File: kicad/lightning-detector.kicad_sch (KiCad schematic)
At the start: 26 parts, among them J1 PWR, J2 Conn_Coaxial, J3 PWR, J4 PWR, J5 RF Detect, U1 NUCLEO-L432KC, U2 AZ1117H-ADJ, U3 TPS61023DRLR

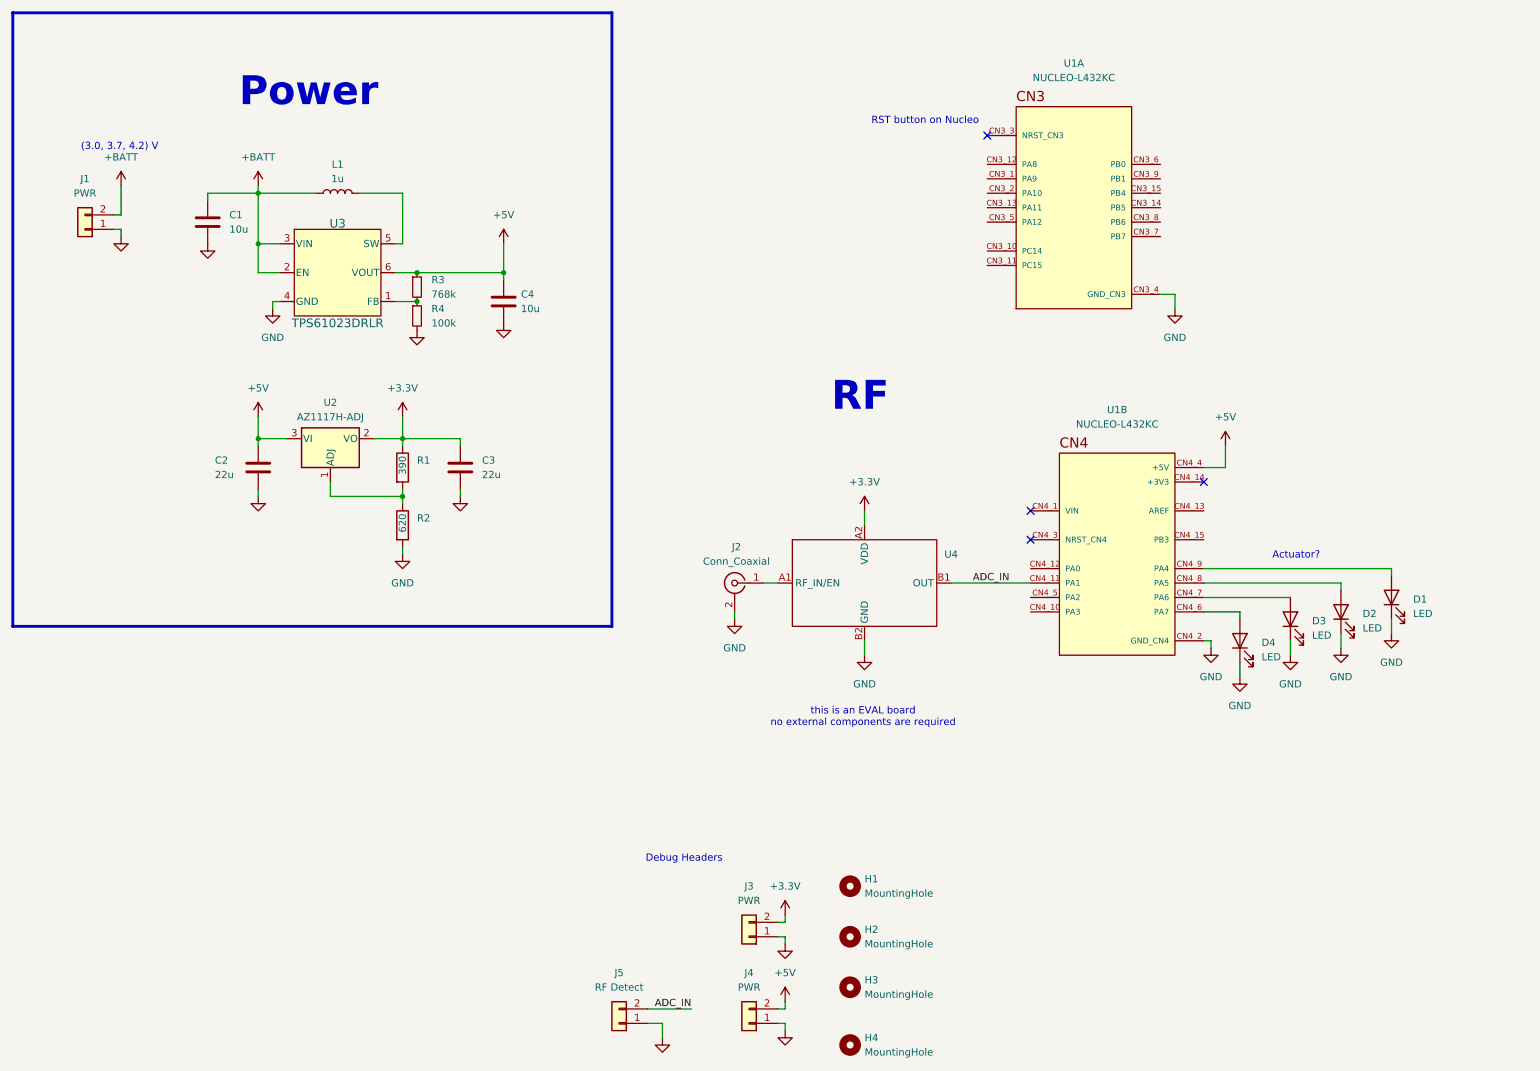
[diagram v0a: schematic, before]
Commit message: Updated schematic and created preliminary PCB.
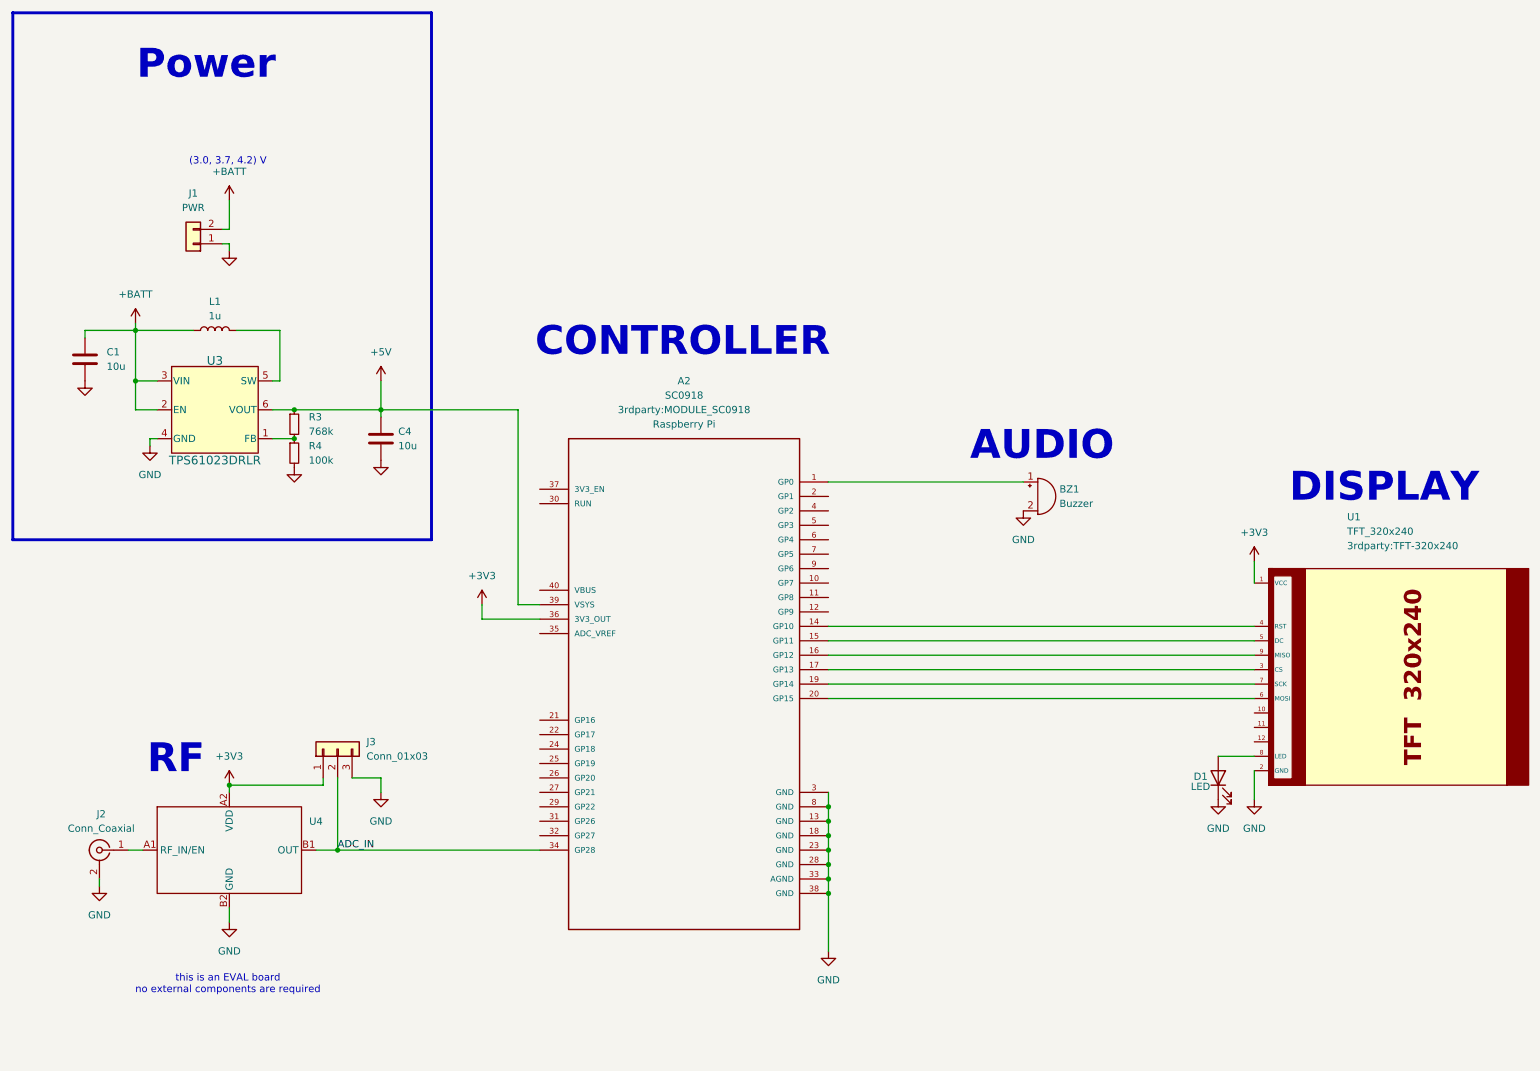
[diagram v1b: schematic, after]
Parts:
- removed C2, C3: 22u, Capacitor_SMD:C_0603_1608Metric, symbol Device:C
- removed D2, D3, D4: LED, symbol Device:LED
- removed H1, H2, H3, H4: MountingHole, MountingHole:MountingHole_4.3mm_M4, symbol Mechanical:MountingHole
- removed J3, J4: PWR, Connector_PinHeader_2.54mm:PinHeader_1x02_P2.54mm_Vertical, symbol Connector_Generic:Conn_01x02
- removed J5: RF Detect, Connector_PinHeader_2.54mm:PinHeader_1x02_P2.54mm_Vertical, symbol Connector_Generic:Conn_01x02
- removed R1: 390, Resistor_SMD:R_0603_1608Metric, symbol Device:R
- removed R2: 620, Resistor_SMD:R_0603_1608Metric, symbol Device:R
- removed U1: NUCLEO-L432KC, NUCLEO-L432KC:MODULE_NUCLEO-L432KC, symbol NUCLEO-L432KC:NUCLEO-L432KC
- removed U2: AZ1117H-ADJ, Package_TO_SOT_SMD:SOT-223-3_TabPin2, symbol Regulator_Linear:AZ1117H-ADJ
- added A2: SC0918, 3rdparty:MODULE_SC0918, symbol Raspberry_Pi_Pico_W_SC0918:SC0918
- added BZ1: Buzzer, Buzzer_Beeper:Buzzer_12x9.5RM7.6, symbol Device:Buzzer
- added J3: Conn_01x03, Connector_PinHeader_2.54mm:PinHeader_1x03_P2.54mm_Vertical, symbol Connector_Generic:Conn_01x03
- added U1: TFT_320x240, 3rdparty:TFT-320x240, symbol tft_320x240:TFT_320x240
- D1: footprint (none) -> LED_THT:LED_D3.0mm
- U3: footprint DRL0006A -> 3rdparty:SOT563-ORI
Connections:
- net +5V: now also A2.39 (VSYS)
- net ADC_IN: now also A2.34 (GP28), J3.2 (Pin_2)
- net GND: now also A2.13 (GND), A2.18 (GND), A2.23 (GND), A2.28 (GND), A2.3 (GND), A2.33 (AGND), A2.38 (GND), A2.8 (GND), BZ1.2 (-), J3.3 (Pin_3), U1.2 (GND)
- net at D1.2 (A): now also U1.8 (LED)
- net +3.3V renamed +3V3
- net +3V3: now also A2.36 (3V3_OUT), J3.1 (Pin_1), U1.1 (VCC)
- new net: A2.1 (GP0), BZ1.1 (+)
- new net: A2.14 (GP10), U1.4 (RST)
- new net: A2.15 (GP11), U1.5 (DC)
- new net: A2.16 (GP12), U1.9 (MISO)
- new net: A2.17 (GP13), U1.3 (CS)
- new net: A2.19 (GP14), U1.7 (SCK)
- new net: A2.20 (GP15), U1.6 (MOSI)
- no-connect marks 4 -> 0
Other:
- note added: "AUDIO"
- note added: "CONTROLLER"
- note added: "DISPLAY"
- note removed: "Actuator?"
- note removed: "Debug Headers"
- note removed: "RST button on Nucleo"
- moved on the sheet: C1, C4, J1, J2, L1, R3, R4, U3, U4

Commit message: wk07 items
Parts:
- removed D1: LED, LED_THT:LED_D3.0mm, symbol Device:LED
- removed U1: TFT_320x240, 3rdparty:TFT-320x240, symbol tft_320x240:TFT_320x240
- added J4: ADF7020 Breakout, Connector_IDC:IDC-Header_2x07_P2.54mm_Vertical, symbol Connector_Generic:Conn_02x07_Top_Bottom
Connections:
- net +3V3: now also J4.3 (Pin_3)
- net GND: now also J4.2 (Pin_2)
- net CLKOUT: now reaches A2.14 (GP10)
- net CLKOUT: now also J4.4 (Pin_4)
- net TXRXCLK: now reaches A2.15 (GP11)
- net TXRXCLK: now also J4.5 (Pin_5)
- net TXRXDATA: now reaches A2.16 (GP12)
- net TXRXDATA: now also J4.6 (Pin_6)
- net SWD_INT: now reaches A2.17 (GP13)
- net SWD_INT: now also J4.7 (Pin_7)
- net CE_70XX: now reaches A2.19 (GP14)
- net CE_70XX: now also J4.14 (Pin_14)
- net ADC_IP: now reaches A2.2 (GP1)
- net ADC_IP: now also J4.8 (Pin_8)
- net SCLK: now reaches A2.4 (GP2)
- net SCLK: now also J4.9 (Pin_9)
- net SREAD: now reaches A2.5 (GP3)
- net SREAD: now also J4.10 (Pin_10)
- net SDATA: now reaches A2.6 (GP4)
- net SDATA: now also J4.11 (Pin_11)
- net SLE: now reaches A2.7 (GP5)
- net SLE: now also J4.12 (Pin_12)
- net MUXOUT: now reaches A2.9 (GP6)
- net MUXOUT: now also J4.13 (Pin_13)
- no-connect marks 0 -> 1
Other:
- note removed: "DISPLAY"
- moved on the sheet: BZ1

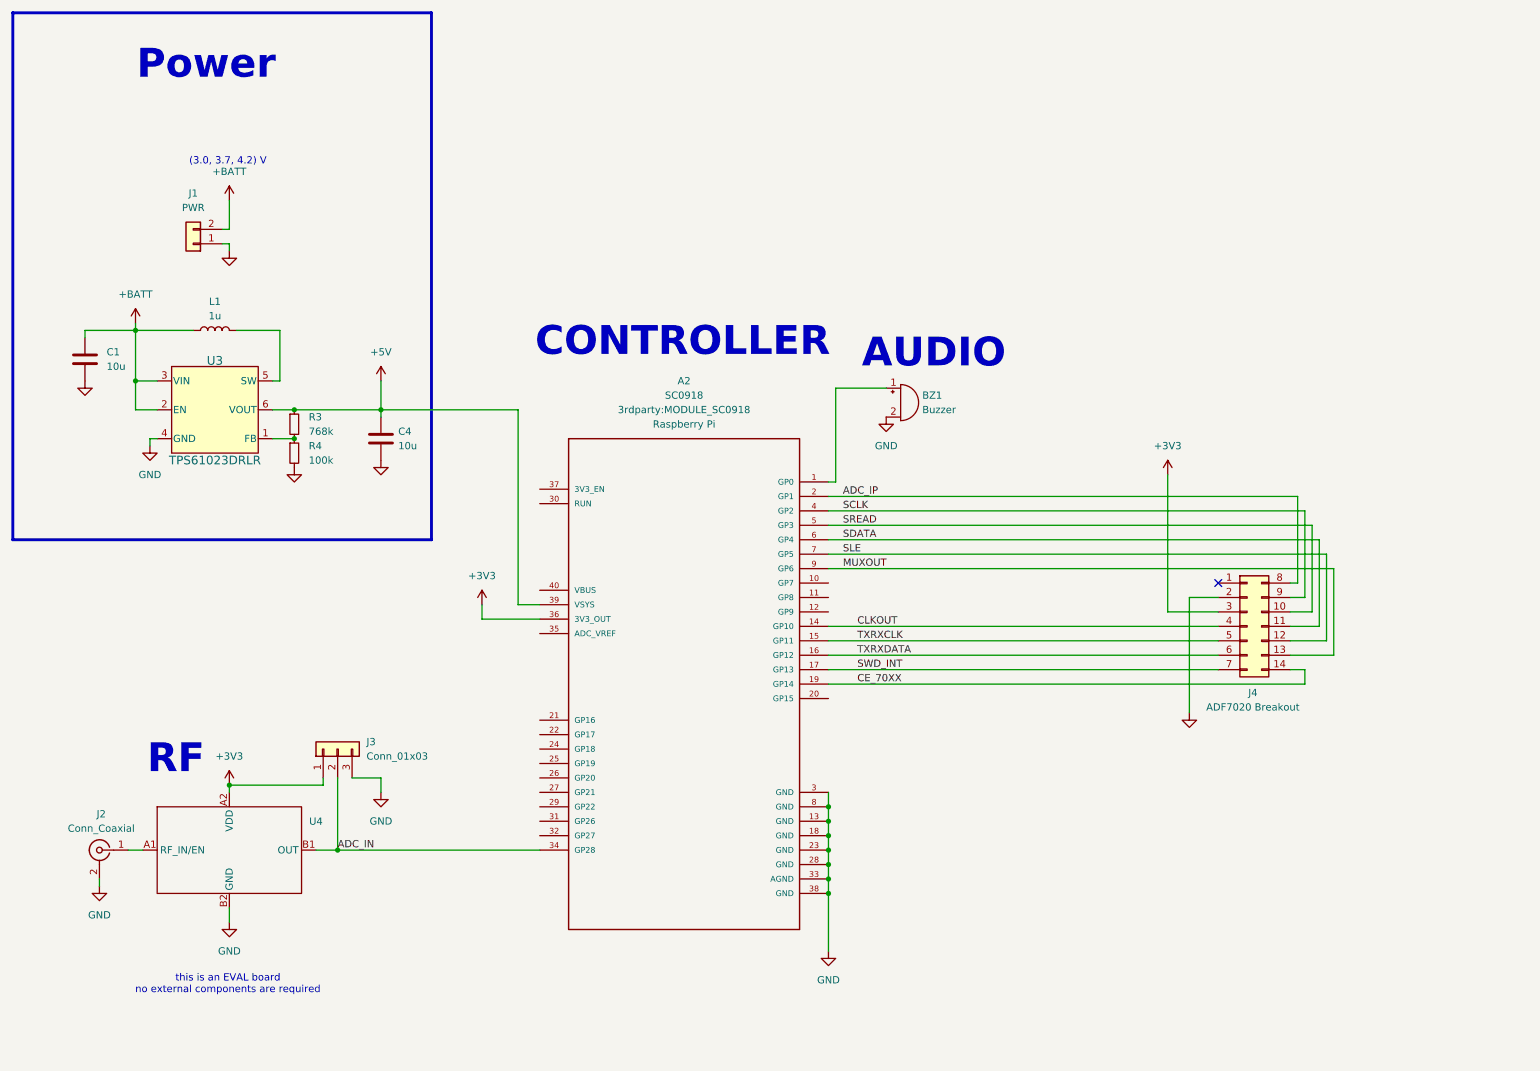
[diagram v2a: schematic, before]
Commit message: v1.1, new schematic/pcb
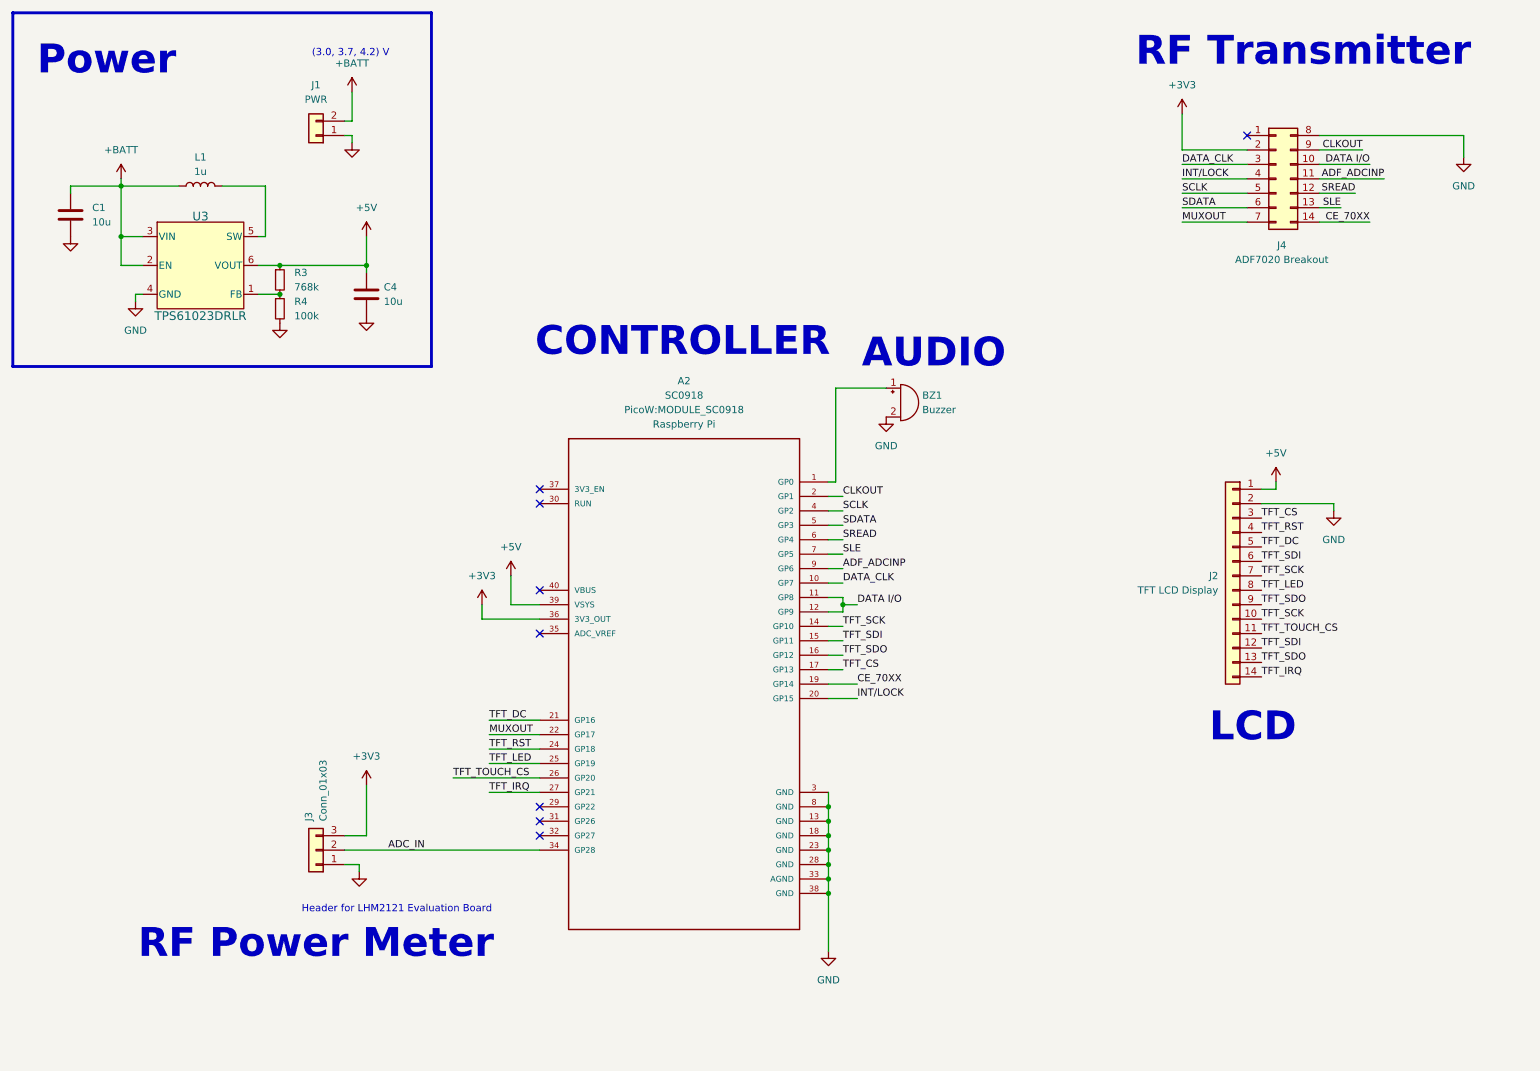
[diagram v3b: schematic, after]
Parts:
- removed J2: Conn_Coaxial, symbol Connector:Conn_Coaxial
- removed U4: ~, symbol LMH2121:LMH2121
- added J2: TFT LCD Display, Connector_PinHeader_2.54mm:PinHeader_1x14_P2.54mm_Vertical, symbol Connector_Generic:Conn_01x14
- A2: footprint 3rdparty:MODULE_SC0918 -> PicoW:MODULE_SC0918
- U3: footprint 3rdparty:SOT563-ORI -> ThunderBuddies_Lib:SOT563-ORI
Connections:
- net +3V3: now also J3.3 (Pin_3), J4.2 (Pin_2); no longer J3.1 (Pin_1), J4.3 (Pin_3)
- net +5V: now also J2.1 (Pin_1)
- net CLKOUT: now also A2.2 (GP1), J4.9 (Pin_9); no longer A2.14 (GP10), J4.4 (Pin_4)
- net GND: now also J3.1 (Pin_1), J4.8 (Pin_8), J2.2 (Pin_2); no longer J3.3 (Pin_3), J4.2 (Pin_2)
- net MUXOUT: now also A2.22 (GP17), J4.7 (Pin_7); no longer A2.9 (GP6), J4.13 (Pin_13)
- net SCLK: now also J4.5 (Pin_5); no longer J4.9 (Pin_9)
- net SDATA: now also A2.5 (GP3), J4.6 (Pin_6); no longer A2.6 (GP4), J4.11 (Pin_11)
- net SLE: now also J4.13 (Pin_13); no longer J4.12 (Pin_12)
- net SREAD: now also A2.6 (GP4), J4.12 (Pin_12); no longer A2.5 (GP3), J4.10 (Pin_10)
- net DATA_CLK: now reaches A2.10 (GP7)
- net DATA_CLK: now also J4.3 (Pin_3)
- net DATA I/O: now reaches A2.11 (GP8)
- net DATA I/O: now also A2.12 (GP9), J4.10 (Pin_10)
- net INT/LOCK: now reaches A2.20 (GP15)
- net INT/LOCK: now also J4.4 (Pin_4)
- net TFT_DC: now reaches A2.21 (GP16)
- net TFT_DC: now also J2.5 (Pin_5)
- net TFT_RST: now reaches A2.24 (GP18)
- net TFT_RST: now also J2.4 (Pin_4)
- net TFT_LED: now reaches A2.25 (GP19)
- net TFT_LED: now also J2.8 (Pin_8)
- net TFT_TOUCH_CS: now reaches A2.26 (GP20)
- net TFT_TOUCH_CS: now also J2.11 (Pin_11)
- net TFT_IRQ: now reaches A2.27 (GP21)
- net TFT_IRQ: now also J2.14 (Pin_14)
- removed net ADC_IP: A2.2 (GP1), J4.8 (Pin_8)
- net SWD_INT renamed TFT_CS
- net TFT_CS: now also J2.3 (Pin_3); no longer J4.7 (Pin_7)
- net TXRXCLK renamed TFT_SDI
- net TFT_SDI: now also J2.12 (Pin_12), J2.6 (Pin_6); no longer J4.5 (Pin_5)
- net TXRXDATA renamed TFT_SDO
- net TFT_SDO: now also J2.13 (Pin_13), J2.9 (Pin_9); no longer J4.6 (Pin_6)
- new net ADF_ADCINP: A2.9 (GP6), J4.11 (Pin_11)
- new net TFT_SCK: A2.14 (GP10), J2.10 (Pin_10), J2.7 (Pin_7)
- no-connect marks 1 -> 8
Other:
- note added: "Header for LHM2121 Evaluation Board"
- note added: "LCD"
- note added: "RF Power Meter"
- note added: "RF Transmitter"
- note removed: "RF"
- note removed: "this is an EVAL board no external components are required"
- moved on the sheet: C1, C4, J1, J3, J4, L1, R3, R4, U3
